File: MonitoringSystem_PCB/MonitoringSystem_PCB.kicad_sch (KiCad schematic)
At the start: 8 parts

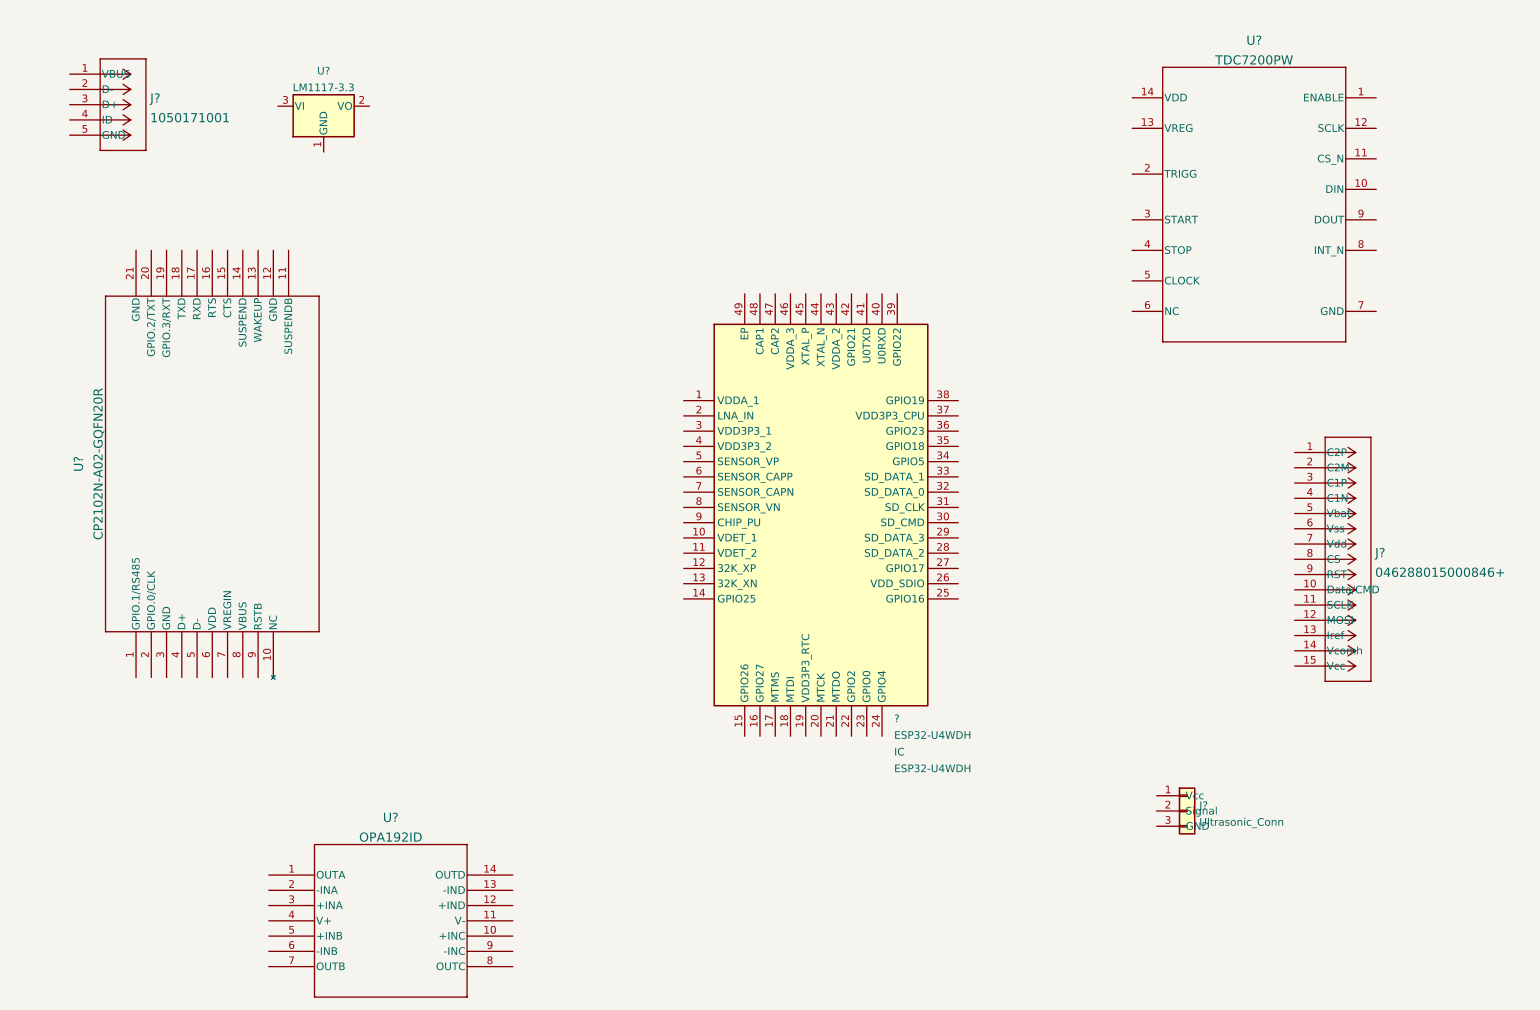
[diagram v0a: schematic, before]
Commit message: redid project bc kicad is braindead
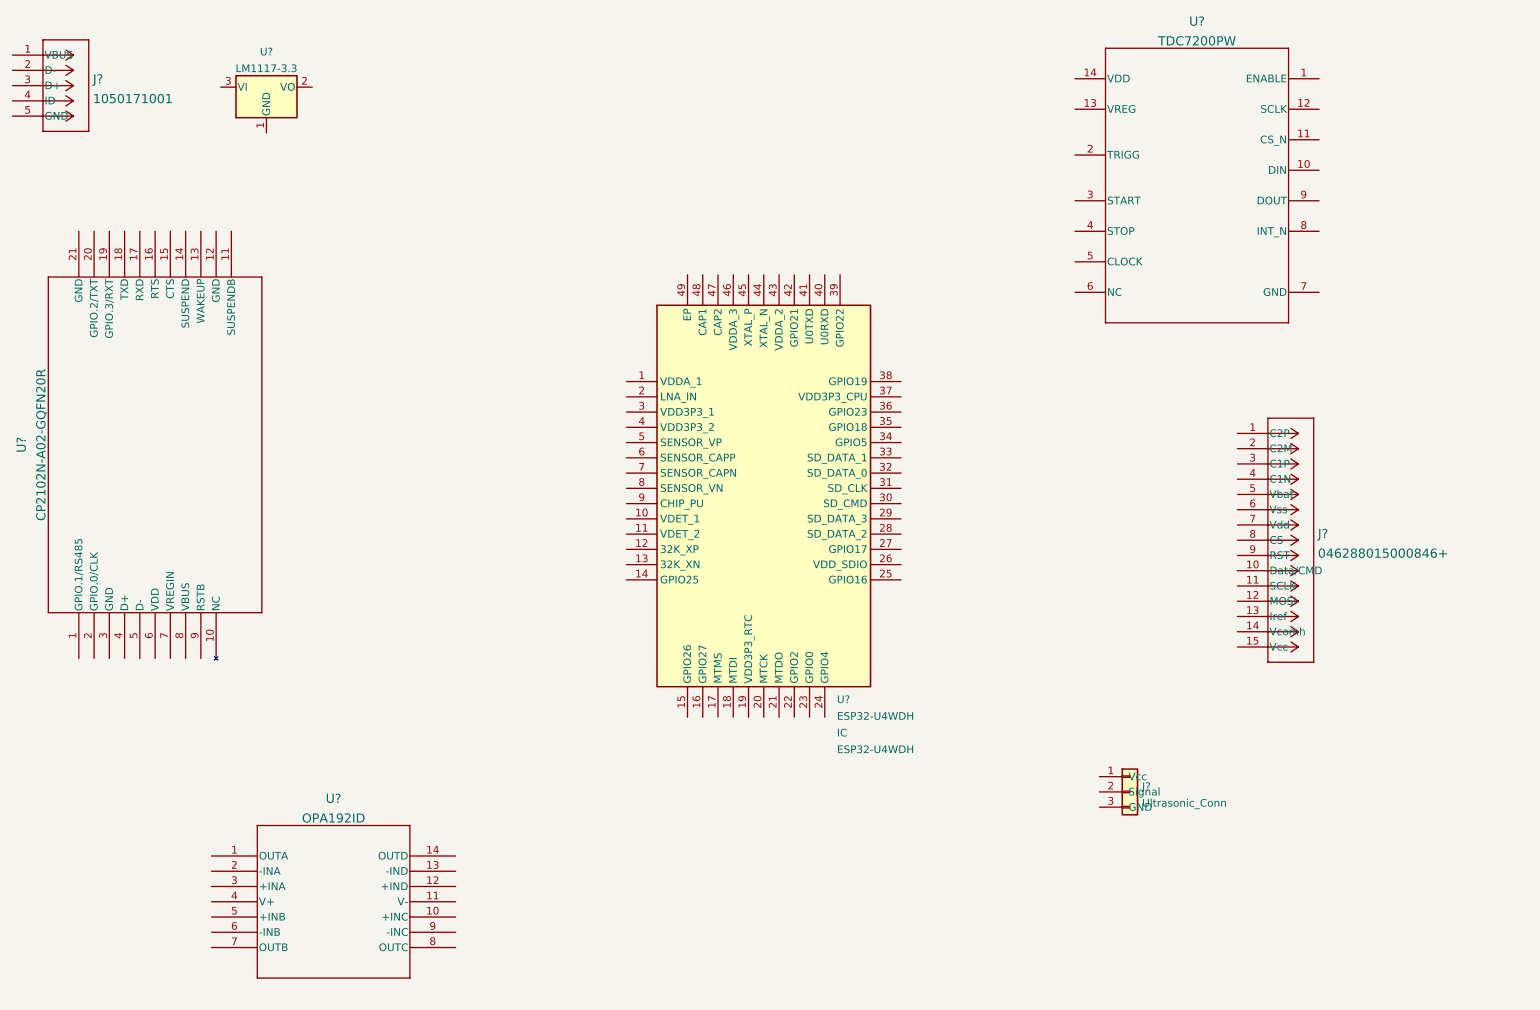
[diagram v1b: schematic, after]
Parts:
- removed ?: ESP32-U4WDH, symbol ESP32-U4WDH:ESP32-U4WDH
- removed J?: Ultrasonic_Conn, symbol Connector_Generic:Conn_01x03
- removed J?: 046288015000846+, CONN15_6288_7X5P7_AVX, symbol 15-pin_ZIF_connector:046288015000846+
- removed J?: 1050171001, CON00679_5_MOL, symbol micro-usb_connector:1050171001
- removed U?: CP2102N-A02-GQFN20R, QFN20_SIL, symbol CP2102-GMR:CP2102N-A02-GQFN20R
- removed U?: TDC7200PW, PW0014A_N, symbol time-to-DC:TDC7200PW
- removed U?: LM1117-3.3, symbol Regulator_Linear:LM1117-3.3
- removed U?: OPA192ID, D14_TEX, symbol op-amp OPA192ID:OPA192ID
- added J?: 046288015000846+, CONN15_6288_7X5P7_AVX, symbol 15-pin_ZIF_connector:046288015000846+
- added J?: Ultrasonic_Conn, symbol Connector_Generic:Conn_01x03
- added J?: 1050171001, CON00679_5_MOL, symbol micro-usb_connector:1050171001
- added U?: LM1117-3.3, symbol Regulator_Linear:LM1117-3.3
- added U?: CP2102N-A02-GQFN20R, QFN20_SIL, symbol CP2102-GMR:CP2102N-A02-GQFN20R
- added U?: TDC7200PW, PW0014A_N, symbol time-to-DC:TDC7200PW
- added U?: ESP32-U4WDH, symbol ESP32-U4WDH:ESP32-U4WDH
- added U?: OPA192ID, D14_TEX, symbol op-amp OPA192ID:OPA192ID
